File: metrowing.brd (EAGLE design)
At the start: 68.6 x 53.5 mm, 8 parts, among them SW1 SPST_TACT-KMR2, U2 ARDUINOR3-NOSILK

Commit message: correct (mkii) version
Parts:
- removed SW1: SPST_TACT-KMR2, adafruit:KMR2
- removed U$3, U$4: FIDUCIAL, adafruit:FIDUCIAL_1MM
- removed U2: ARDUINOR3-NOSILK, microbuilder:ARDUINOR3-NOSILK
- added S1: MOMENTARY-SWITCH-SPST-SMD-6.0X3.5MM, SparkFun-Switches:TACTILE_SWITCH_SMD_6.0X3.5MM
- added U1: ARDUINOR3-DIMENSION, 00_bsiepert:ARDUINOR3
- J1: device SparkFun-Connectors:1X16 -> SparkFun-Connectors:1X12
- J2: device SparkFun-Connectors:1X12 -> SparkFun-Connectors:1X16
- MS1, MS2: value FEATHERWING_NODIM -> FEATHERWING_PINS; device microbuilder:FEATHERWING_DIM -> 00_bsiepert:FEATHERWING_PINS
- moved J1 37.7 mm to (63.6, 10.7), turned to 90 degrees
- moved J2 9.52 mm to (53.5, 43.8)
- moved MS2 2.59 mm to (26.7, 50.2)
- moved MS1 1.50 mm to (1.41, 50.2)
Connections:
- removed net 3V: J1.2, MS1.2, MS2.2, U2.3V
- removed net N$5: J2.2, MS1.27, MS2.27
- removed net RST: J1.1, MS1.1, MS2.1
- removed net VIN: U2.VIN
- new net 3V3: J2.2, MS1.2, MS2.2, U1.3V
- new net D2: U1.D2
- new net D3: U1.D3
- new net D4: U1.D4
- new net D7: U1.D7
- new net D8: U1.D8
- new net ENABLE: J1.11, MS1.27, MS2.27
- new net IOREF: U1.IOREF
- new net N$153: U1.VIN
- new net N$4: U1.RESERVED
- net +5V: now also U1.5V; no longer U2.5V
- net A0: now also J2.5, U1.A0; no longer J1.5, U2.A0
- net A1: now also J2.6, U1.A1; no longer J1.6, U2.A1
- net A2: now also J2.7, U1.A2; no longer J1.7, U2.A2
- net A3: now also J2.8, U1.A3; no longer J1.8, U2.A3
- net A4: now also J2.9, U1.A4; no longer J1.9, U2.A4
- net A5: now also J2.10, U1.A5; no longer J1.10, U2.A5
- net AREF: now also J2.3, U1.AREF; no longer J1.3, U2.AREF
- net D0: now also J2.14, U1.D0; no longer J1.14, U2.D0
- net D1: now also J2.15, U1.D1; no longer J1.15, U2.D1
- net D10: now also J1.6, U1.D10; no longer J2.7
- net D11: now also J1.7, U1.D11; no longer J2.6
- net D12: now also J1.8, U1.D12; no longer J2.5
- net D13: now also J1.9, U1.D13; no longer J2.4
- net D5: now also J1.3, U1.D5; no longer J2.10
- net D6: now also J1.4, U1.D6; no longer J2.9
- net D9: now also J1.5, U1.D9; no longer J2.8
- net GND: now also J2.16, J2.4, S1.1, U1.GND, U1.GND1, U1.GND2; no longer J1.16, J1.4, SW1.1, SW1.3, U2.GND, U2.GND1, U2.GND2
- net MISO: now also J2.13; no longer J1.13
- net MOSI: now also J2.12; no longer J1.12
- net RESET: now also J2.1, MS1.1, MS2.1, S1.2, U1.RESET; no longer SW1.2, SW1.4, U2.RESET
- net SCK: now also J2.11; no longer J1.11
- net SCL: now also J1.2, U1.SCL; no longer J2.11, U2.SCL
- net SDA: now also J1.1, U1.SDA; no longer J2.12, U2.SDA
- net USB: now also J1.10; no longer J2.3
- net VBAT: now also J1.12; no longer J2.1
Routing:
- net RESET: track 4.00 -> 130.1 mm
- net 3V3: track 0.00 -> 98.9 mm, vias 0 -> 1
- net D1: track 20.8 -> 100.6 mm, vias 0 -> 1
- net D0: track 20.8 -> 99.7 mm, vias 0 -> 1
- net SDA: track 20.9 -> 91.1 mm
- net SCL: track 20.8 -> 88.0 mm
- net GND: track 39.9 -> 103.5 mm, vias 7 -> 0
- net D10: track 20.8 -> 84.2 mm, vias 0 -> 1
- net D5: track 21.4 -> 84.6 mm
- net D9: track 20.8 -> 84.0 mm
- net A0: track 22.3 -> 85.2 mm, vias 0 -> 1
- net D11: track 20.8 -> 82.7 mm, vias 0 -> 1
- net D6: track 20.8 -> 82.3 mm
- net A1: track 22.3 -> 82.7 mm, vias 0 -> 1
- net A2: track 22.3 -> 81.9 mm, vias 0 -> 1
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- removed copper zone on layer 1, net N$4
- removed copper zone on layer 1, net VBAT
- removed copper zone on layer 1, net VOUT
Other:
- board size 68.6 x 53.5 mm -> 68.6 x 53.3 mm
- board text added: "A0"
- board text added: "A1"
- board text added: "A2"
- board text added: "A3"
- board text added: "A4"
- board text added: "A5"
- board text added: "BAT"
- board text added: "D0"
- board text added: "D1"
- board text added: "D10"
- board text added: "D11"
- board text added: "D12"
- board text added: "D13"
- board text added: "D5"
- board text added: "D6"
- board text added: "D9"
- board text added: "EN"
- board text added: "GND"
- board text added: "MISO"
- board text added: "MOSI"
- board text added: "SCK"
- board text added: "USB"
- board text removed: "0"
- board text removed: "1"
- board text removed: "2"
- board text removed: "3"
- board text removed: "4"
- board text removed: "5"
- board text removed: "6"
- board text removed: "7"
- board text removed: "8"
- board text removed: "ARef"
- board text removed: "Vin"
- board text removed: "gnd"

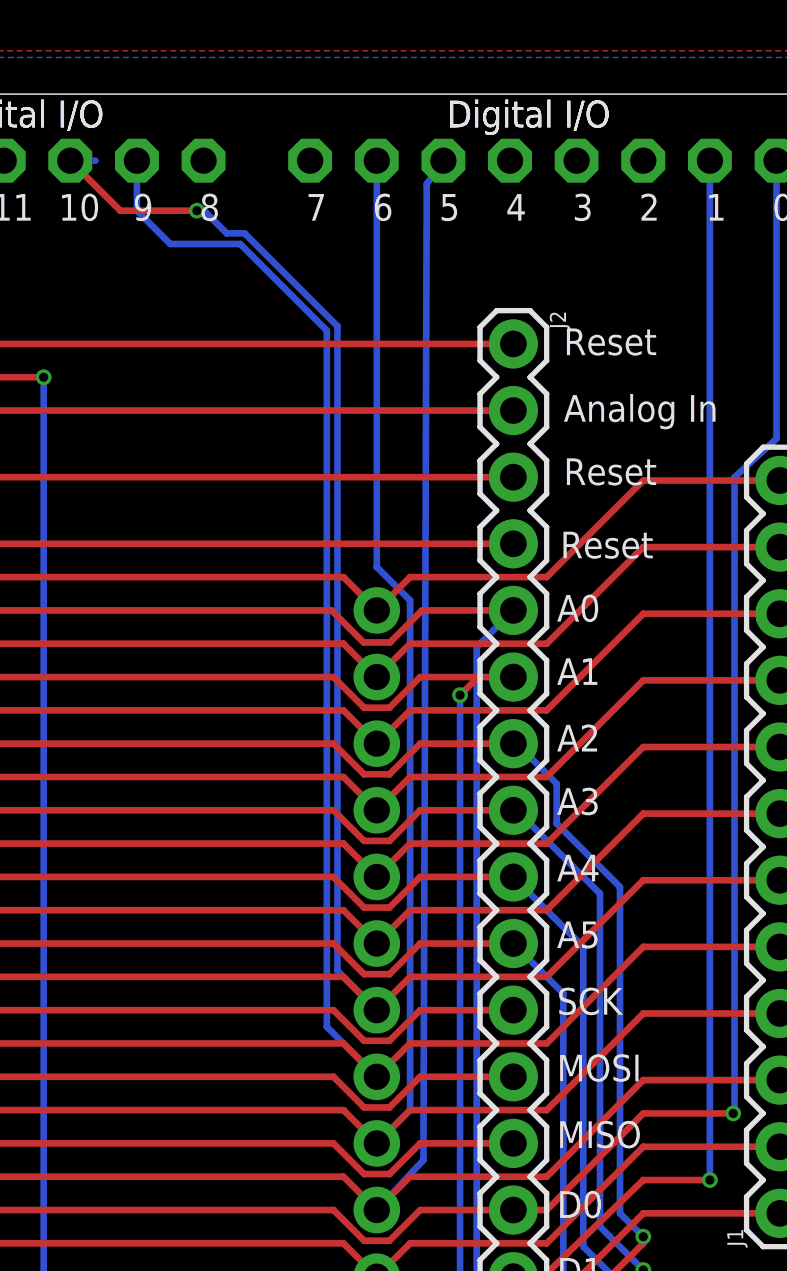
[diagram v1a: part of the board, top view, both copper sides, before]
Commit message: fixed clearance drc
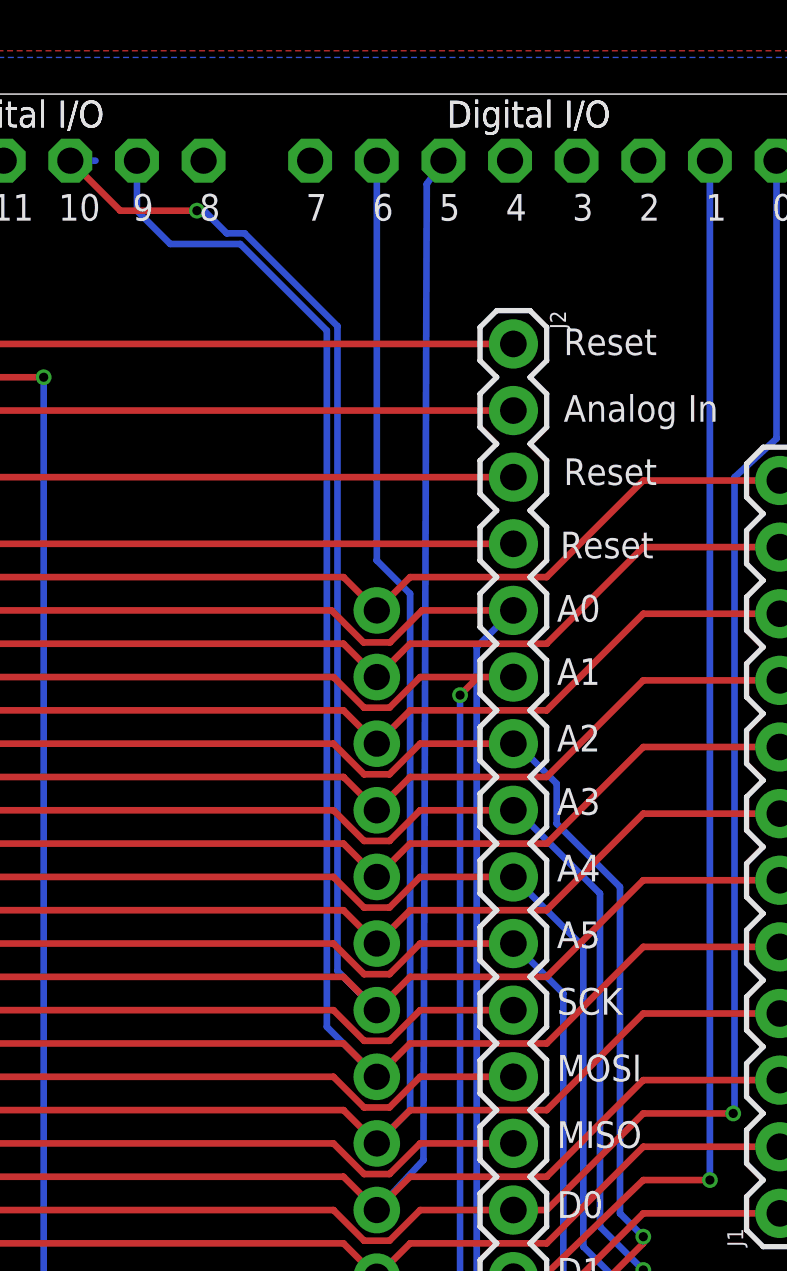
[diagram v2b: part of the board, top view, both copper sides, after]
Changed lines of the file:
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@@
 <wire x1="22.7584" y1="35.06376875" x2="21.8286" y2="34.13396875" width="0.254" layer="16"/>
 <wire x1="22.7584" y1="35.06376875" x2="22.7584" y2="45.67493125" width="0.254" layer="16"/>
-<wire x1="34.036" y1="50.8" x2="33.07653125" y2="50.8" width="0" layer="19" extent="1-16"/>
 <wire x1="21.8286" y1="34.13396875" x2="21.8286" y2="23.00603125" width="0.254" layer="16"/>
 <via x="22.7584" y="45.67493125" extent="1-16" drill="0.35"/>
@@
 <wire x1="21.34463125" y1="33.65" x2="2.677" y2="33.65" width="0.254" layer="1"/>
 <wire x1="53.467" y1="33.655" x2="52.07" y2="32.258" width="0.254" layer="16"/>
-<wire x1="50.8" y1="3.429" x2="50.8" y2="2.54" width="0" layer="19" extent="1-16"/>
 <wire x1="52.07" y1="4.445" x2="52.324" y2="4.191" width="0.254" layer="16"/>
 <via x="52.324" y="4.191" extent="1-16" drill="0.35"/>
@@
 <wire x1="22.51303125" y1="29.9416" x2="21.34463125" y2="31.11" width="0.254" layer="1"/>
 <wire x1="21.34463125" y1="31.11" x2="2.677" y2="31.11" width="0.254" layer="1"/>
-<wire x1="53.086" y1="2.54" x2="53.34" y2="2.54" width="0" layer="19" extent="1-16"/>
-<wire x1="53.086" y1="2.54" x2="52.38053125" y2="2.54" width="0" layer="19" extent="1-16"/>
 <via x="51.435" y="30.4264" extent="1-16" drill="0.35"/>
 <wire x1="51.435" y1="30.4264" x2="52.1236" y2="31.115" width="0.254" layer="1"/>
@@
 <wire x1="46.99" y1="14.605" x2="48.26" y2="13.335" width="0.254" layer="1"/>
 <wire x1="24.272" y1="14.605" x2="46.99" y2="14.605" width="0.254" layer="1"/>
-<wire x1="48.26" y1="35.30736875" x2="48.26" y2="50.8" width="0.254" layer="16"/>
-<wire x1="48.26" y1="35.306" x2="48.26" y2="35.30736875" width="0.254" layer="16"/>
+<wire x1="48.26" y1="35.56136875" x2="48.26" y2="50.8" width="0.254" layer="16"/>
+<wire x1="48.26" y1="35.56" x2="48.26" y2="35.56136875" width="0.254" layer="16"/>
 <wire x1="48.26" y1="13.335" x2="49.53" y2="14.605" width="0.254" layer="16"/>
-<wire x1="49.53" y1="14.605" x2="49.53" y2="34.036" width="0.254" layer="16"/>
-<wire x1="49.53" y1="34.036" x2="48.26" y2="35.306" width="0.254" layer="16"/>
+<wire x1="49.53" y1="14.605" x2="49.53" y2="34.29" width="0.254" layer="16"/>
+<wire x1="49.53" y1="34.29" x2="48.26" y2="35.56" width="0.254" layer="16"/>
 </signal>
 <signal name="D7">

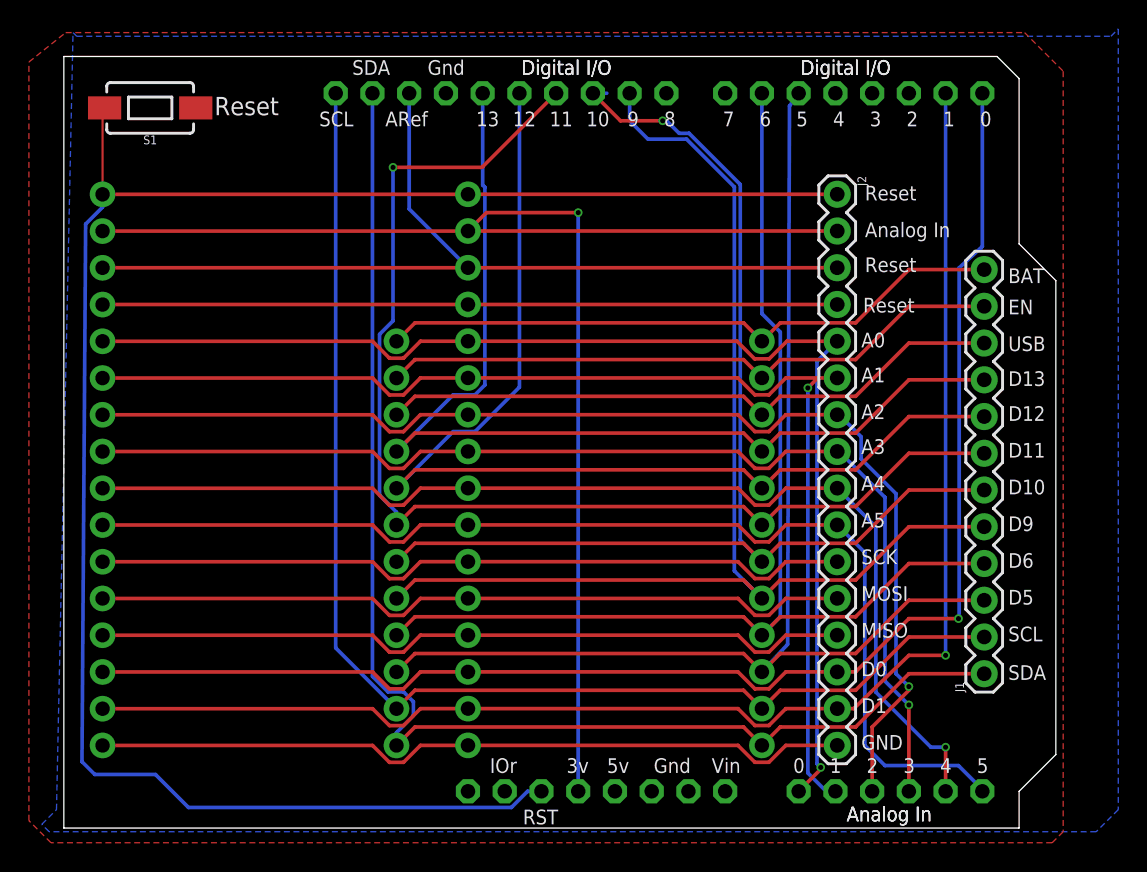
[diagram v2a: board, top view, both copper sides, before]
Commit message: updated and fixed mkii: Now with more SPI
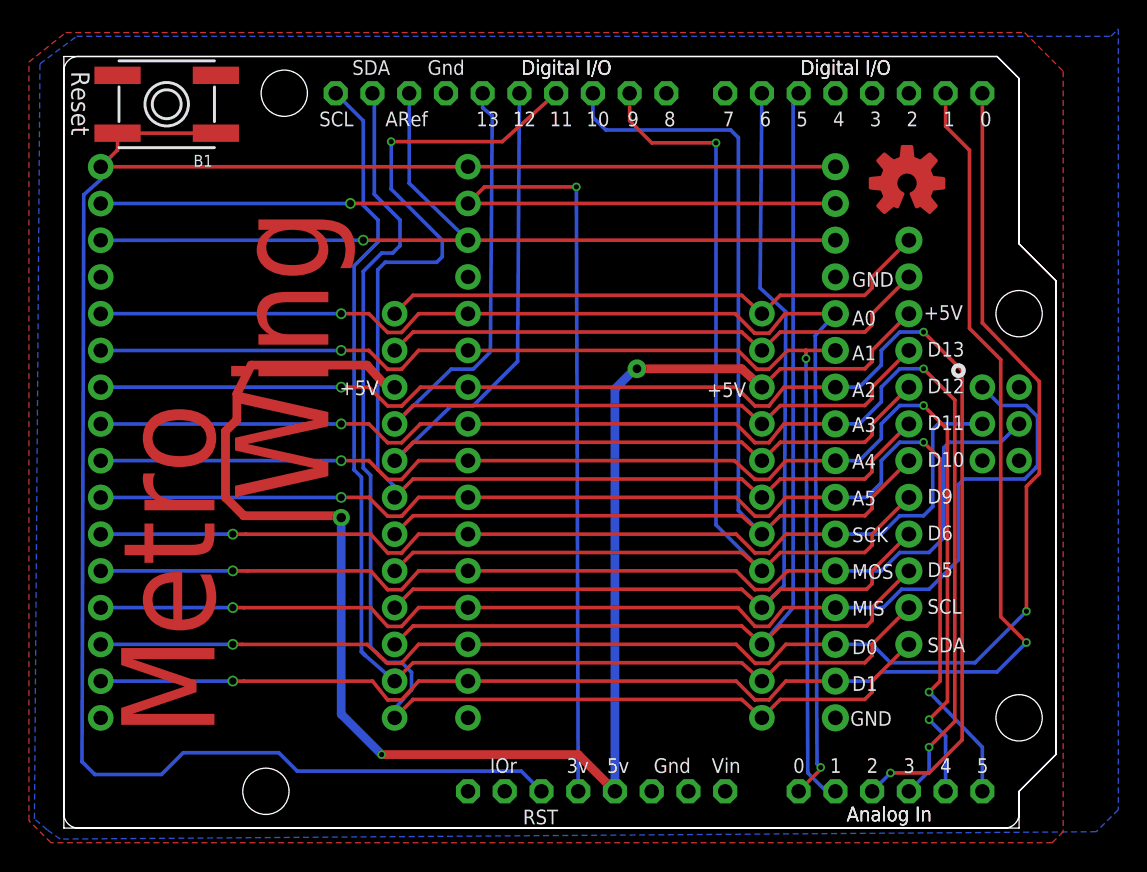
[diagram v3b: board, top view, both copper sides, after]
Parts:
- removed S1: MOMENTARY-SWITCH-SPST-SMD-6.0X3.5MM, SparkFun-Switches:TACTILE_SWITCH_SMD_6.0X3.5MM
- added B1: (no value), microbuilder:EVQ-Q2
- added ICSP1: 3x2 M, microbuilder:2X03_ROUND_70MIL
- added U$1: (no value), adafruit:OSHWLOGO_TOP_0.2
- moved J1 5.59 mm to (58.4, 12.7)
- moved MS1 1.91 mm to (1.28, 52.1)
- moved J2 1.91 mm to (53.3, 45.7)
- moved MS2 1.91 mm to (26.7, 52.1)
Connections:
- removed net USB: J1.10, MS1.26, MS2.26
- new net VCCIO: ICSP1.2
- net +5V: now also J1.10, MS1.26, MS2.26
- net GND: now also B1.A, B1.A', ICSP1.6; no longer S1.1
- net MISO: now also ICSP1.1
- net MOSI: now also ICSP1.4
- net RESET: now also B1.B, B1.B'; no longer S1.2
- net SCK: now also ICSP1.3
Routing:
- net +5V: track 0.00 -> 115.3 mm, vias 0 -> 3
- net GND: track 103.5 -> 0.01 mm
- net USB: track 43.7 -> 0.00 mm
- net MISO: track 52.7 -> 82.3 mm, vias 0 -> 1
- net MOSI: track 52.7 -> 73.6 mm, vias 0 -> 1
- net SCK: track 52.7 -> 69.5 mm, vias 0 -> 1
- net A2: track 81.9 -> 98.5 mm, vias 1 -> 3
- net A3: track 78.3 -> 92.7 mm, vias 1 -> 3
- net A4: track 77.4 -> 89.6 mm, vias 1 -> 3
- net A5: track 78.3 -> 88.1 mm, vias 0 -> 3
- net D1: track 100.6 -> 107.7 mm, vias 1 -> 2
- net D12: track 75.5 -> 69.0 mm
- net D5: track 84.6 -> 78.2 mm
- net D0: track 99.7 -> 106.0 mm, vias 1 -> 2
- net D6: track 82.3 -> 76.2 mm
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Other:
- outline, holes or cut-outs redrawn
- board text added: "+5V"
- board text added: "D:/SmartProjects/Snc/a4_bn_logo2.bmp"
- board text added: "MIS"
- board text added: "MOS"
- board text added: "Metro"
- board text added: "Wing"
- board text removed: "BAT"
- board text removed: "EN"
- board text removed: "MISO"
- board text removed: "MOSI"
- board text removed: "USB"
